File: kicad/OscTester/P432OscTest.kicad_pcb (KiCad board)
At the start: 2 copper layers, 49.5 x 59.7 mm, 12 parts, among them J1 Power-XP6, J2 Freq-XP1, J3 Filter-XP7, J4 Volume-XP6, J5 Control-XP5, SW1 SW_DIP_x04

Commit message: pcb fix
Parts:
- moved J1 7.62 mm to (43.2, 94.0), turned to 270 degrees
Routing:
- net +5V: track 169.9 -> 157.1 mm
- net GND: track 119.4 -> 121.8 mm
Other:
- board text added: "1"
- board text added: "11"
- board text added: "4"
- board text added: "8"
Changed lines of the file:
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@@
   (general
     (thickness 1.6)
-    (drawings 33)
-    (tracks 51)
+    (drawings 43)
+    (tracks 50)
     (zones 0)
     (modules 12)
@@
   )
   (module Connector_PinSocket_2.54mm:PinSocket_1x04_P2.54mm_Vertical (layer F.Cu)
-    (at 35.56 93.98 90)
+    (at 43.18 93.98 270)
     (descr "Through hole straight socket strip, 1x04, 2.54mm pitch, single row (from Kicad 4.0.7), script generated")
     (tags "Through hole socket strip THT 1x04 2.54mm single row")
@@
       (effects (font (size 1 1) (thickness 0.15)))
     )
-    (fp_text value Power-XP6 (at -3.175 3.81 180) (layer F.SilkS)
+    (fp_text value Power-XP6 (at 2.54 3.81 180) (layer F.SilkS)
       (effects (font (size 1 1) (thickness 0.15)))
     )
@@
     (fp_line (start 0.635 -1.27) (end 1.27 -0.635) (layer F.Fab) (width 0.1))
     (fp_line (start -1.27 -1.27) (end 0.635 -1.27) (layer F.Fab) (width 0.1))
-    (pad 4 thru_hole oval (at 0 7.62 90) (size 1.7 1.7) (drill 1) (layers *.Cu *.Mask)
-      (net 1 GND))
-    (pad 3 thru_hole oval (at 0 5.08 90) (size 1.7 1.7) (drill 1) (layers *.Cu *.Mask)
-      (net 1 GND))
-    (pad 2 thru_hole oval (at 0 2.54 90) (size 1.7 1.7) (drill 1) (layers *.Cu *.Mask)
+    (pad 4 thru_hole oval (at 0 7.62 270) (size 1.7 1.7) (drill 1) (layers *.Cu *.Mask)
+      (net 1 GND))
+    (pad 3 thru_hole oval (at 0 5.08 270) (size 1.7 1.7) (drill 1) (layers *.Cu *.Mask)
+      (net 1 GND))
+    (pad 2 thru_hole oval (at 0 2.54 270) (size 1.7 1.7) (drill 1) (layers *.Cu *.Mask)
       (net 2 +5V))
-    (pad 1 thru_hole rect (at 0 0 90) (size 1.7 1.7) (drill 1) (layers *.Cu *.Mask)
+    (pad 1 thru_hole rect (at 0 0 270) (size 1.7 1.7) (drill 1) (layers *.Cu *.Mask)
       (net 2 +5V))
     (model ${KISYS3DMOD}/Connector_PinSocket_2.54mm.3dshapes/PinSocket_1x04_P2.54mm_Vertical.wrl
@@
     )
   )
-  (gr_text GND (at 41.91 91.44) (layer F.SilkS)
-    (effects (font (size 1 1) (thickness 0.15)))
-  )
-  (gr_text +5V (at 36.195 91.44) (layer F.SilkS)
+  (gr_text 4 (at 34.925 91.44) (layer F.SilkS)
+    (effects (font (size 1 1) (thickness 0.25)))
+  )
+  (gr_text 1 (at 43.815 91.44) (layer F.SilkS)
+    (effects (font (size 1 1) (thickness 0.25)))
+  )
+  (gr_text 11 (at 48.26 76.2) (layer F.SilkS)
+    (effects (font (size 1 1) (thickness 0.25)))
+  )
+  (gr_text 1 (at 73.66 76.2) (layer F.SilkS)
+    (effects (font (size 1 1) (thickness 0.25)))
+  )
+  (gr_text 8 (at 55.245 66.04) (layer F.SilkS)
+    (effects (font (size 1 1) (thickness 0.25)))
+  )
+  (gr_text 1 (at 73.66 66.04) (layer F.SilkS)
+    (effects (font (size 1 1) (thickness 0.25)))
+  )
+  (gr_text 8 (at 55.245 55.88) (layer F.SilkS)
+    (effects (font (size 1 1) (thickness 0.25)))
+  )
+  (gr_text 1 (at 73.66 55.88) (layer F.SilkS)
+    (effects (font (size 1 1) (thickness 0.25)))
+  )
+  (gr_text 8 (at 55.88 45.72) (layer F.SilkS)
+    (effects (font (size 1 1) (thickness 0.25)))
+  )
+  (gr_text 1 (at 74.295 45.72) (layer F.SilkS)
+    (effects (font (size 1 1) (thickness 0.25)))
+  )
+  (gr_text GND (at 37.465 91.44) (layer F.SilkS)
+    (effects (font (size 1 1) (thickness 0.15)))
+  )
+  (gr_text +5V (at 41.275 91.44) (layer F.SilkS)
     (effects (font (size 1 1) (thickness 0.15)))
   )
@@
   (segment (start 63.5 78.74) (end 48.26 78.74) (width 0.8) (layer B.Cu) (net 1))
   (segment (start 48.26 78.74) (end 45.72 78.74) (width 0.8) (layer B.Cu) (net 1))
-  (segment (start 43.18 81.28) (end 43.18 93.98) (width 0.8) (layer B.Cu) (net 1))
-  (segment (start 45.72 78.74) (end 43.18 81.28) (width 0.8) (layer B.Cu) (net 1))
-  (segment (start 43.18 93.98) (end 40.64 93.98) (width 0.8) (layer B.Cu) (net 1))
   (segment (start 71.12 48.26) (end 55.88 48.26) (width 0.8) (layer B.Cu) (net 1))
   (segment (start 38.1 49.53) (end 38.1 58.42) (width 0.8) (layer B.Cu) (net 1))
@@
   (segment (start 38.1 58.42) (end 38.1 68.58) (width 0.8) (layer B.Cu) (net 1))
   (segment (start 38.1 68.58) (end 38.1 76.2) (width 0.8) (layer B.Cu) (net 1))
-  (segment (start 38.1 76.2) (end 43.18 81.28) (width 0.8) (layer B.Cu) (net 1))
-  (segment (start 35.56 93.98) (end 38.1 93.98) (width 0.8) (layer B.Cu) (net 2))
+  (segment (start 35.56 93.98) (end 38.1 93.98) (width 0.8) (layer B.Cu) (net 1))
+  (segment (start 38.1 93.98) (end 38.1 86.36) (width 0.8) (layer B.Cu) (net 1))
+  (segment (start 45.72 78.74) (end 39.37 78.74) (width 0.8) (layer B.Cu) (net 1))
+  (segment (start 38.1 76.2) (end 38.1 80.01) (width 0.8) (layer B.Cu) (net 1))
+  (segment (start 39.37 78.74) (end 38.1 80.01) (width 0.8) (layer B.Cu) (net 1))
+  (segment (start 38.1 80.01) (end 38.1 86.36) (width 0.8) (layer B.Cu) (net 1))
   (segment (start 73.66 93.98) (end 66.04 93.98) (width 0.8) (layer B.Cu) (net 2))
-  (segment (start 66.04 93.98) (end 63.5 93.98) (width 0.8) (layer B.Cu) (net 2))
-  (segment (start 63.5 93.98) (end 58.42 99.06) (width 0.8) (layer B.Cu) (net 2))
-  (segment (start 35.56 95.63) (end 35.56 93.98) (width 0.8) (layer B.Cu) (net 2))
-  (segment (start 38.99 99.06) (end 35.56 95.63) (width 0.8) (layer B.Cu) (net 2))
-  (segment (start 58.42 99.06) (end 38.99 99.06) (width 0.8) (layer B.Cu) (net 2))
   (segment (start 73.66 93.98) (end 76.2 93.98) (width 0.8) (layer B.Cu) (net 2))
   (segment (start 76.2 93.98) (end 77.47 92.71) (width 0.8) (layer B.Cu) (net 2))
@@
   (segment (start 48.26 63.5) (end 43.18 68.58) (width 0.8) (layer B.Cu) (net 2))
   (segment (start 77.47 92.71) (end 77.47 63.5) (width 0.8) (layer B.Cu) (net 2))
+  (segment (start 63.5 93.98) (end 43.18 93.98) (width 0.8) (layer B.Cu) (net 2))
+  (segment (start 66.04 93.98) (end 63.5 93.98) (width 0.8) (layer B.Cu) (net 2))
+  (segment (start 43.18 93.98) (end 40.64 93.98) (width 0.8) (layer B.Cu) (net 2))
   (segment (start 66.04 76.2) (end 66.04 78.74) (width 0.8) (layer B.Cu) (net 3))
   (segment (start 66.04 78.74) (end 66.04 86.36) (width 0.8) (layer B.Cu) (net 3))

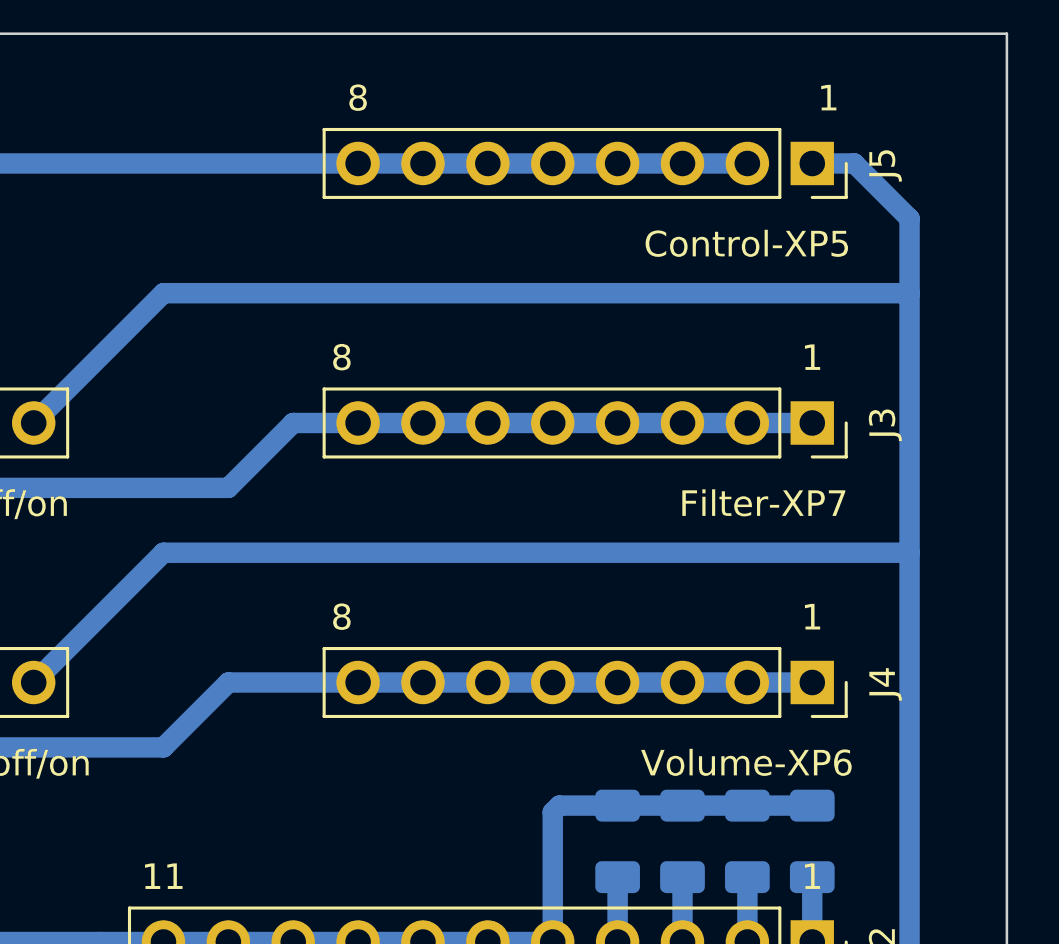
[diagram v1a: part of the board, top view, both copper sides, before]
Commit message: Unison bit set to 0 to test all 8 voices
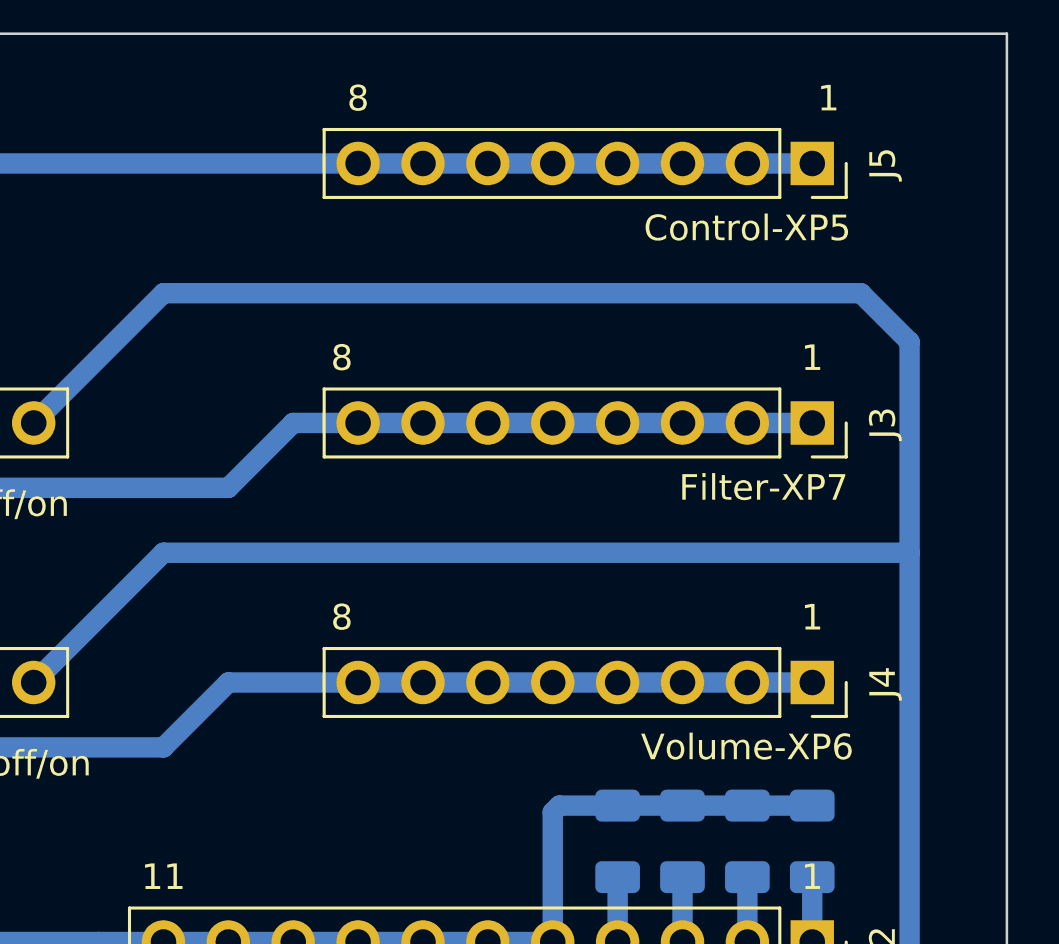
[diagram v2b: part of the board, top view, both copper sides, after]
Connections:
- net /FC0 renamed /1
- net /FC1 renamed /2
- net /FC2 renamed /3
- net /FC3 renamed /4
- J5 pad 1: +5V -> GND
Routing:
- net +5V: track 157.1 -> 148.4 mm
- net GND: track 121.8 -> 124.3 mm

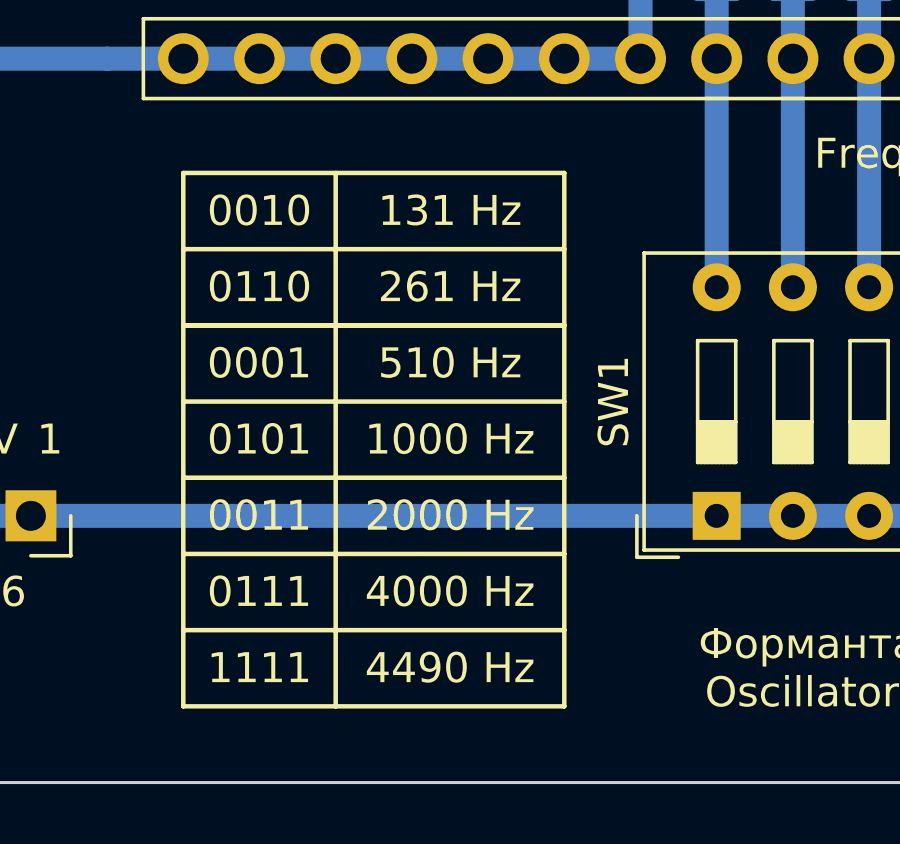
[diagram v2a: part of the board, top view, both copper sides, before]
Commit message: Freq values changed to the correct ones.
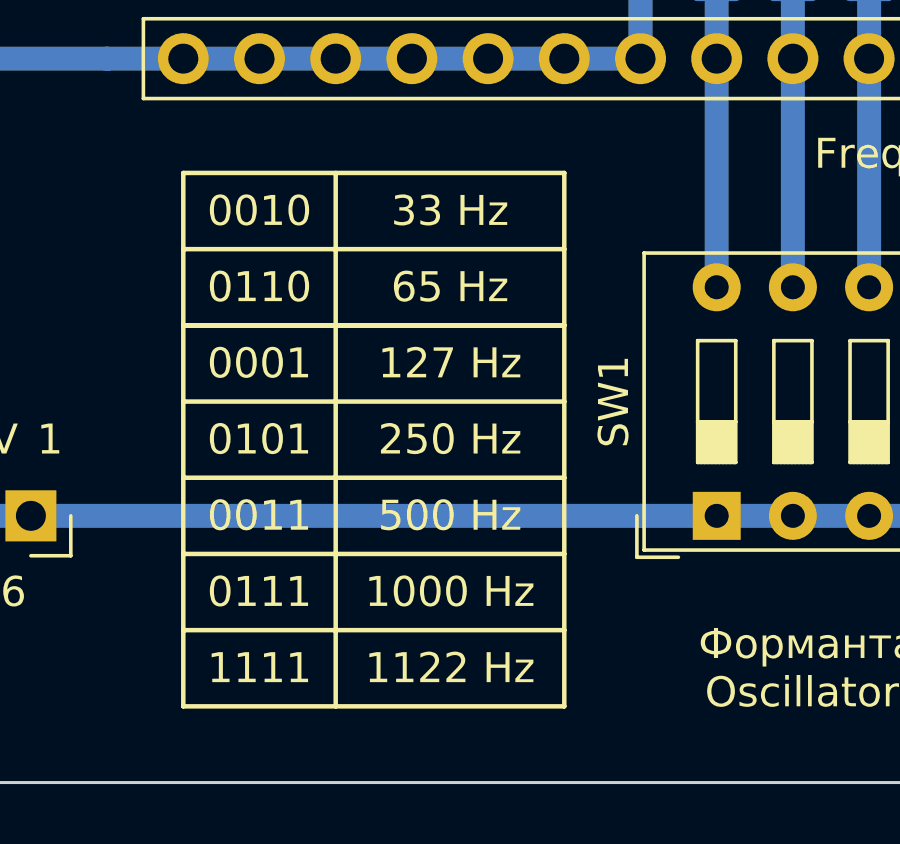
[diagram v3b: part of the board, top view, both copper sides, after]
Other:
- board text added: "1122 Hz"
- board text added: "127 Hz"
- board text added: "250 Hz"
- board text added: "33 Hz"
- board text added: "500 Hz"
- board text added: "65 Hz"
- board text removed: "131 Hz"
- board text removed: "2000 Hz"
- board text removed: "261 Hz"
- board text removed: "4000 Hz"
- board text removed: "4490 Hz"
- board text removed: "510 Hz"
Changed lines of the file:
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@@
     (effects (font (size 1 1) (thickness 0.15)))
   )
-  (gr_text "131 Hz" (at 57.15 83.82) (layer F.SilkS)
+  (gr_text "33 Hz" (at 57.15 83.82) (layer F.SilkS)
     (effects (font (size 1 1) (thickness 0.15)))
   )
-  (gr_text "261 Hz" (at 57.15 86.36) (layer F.SilkS)
+  (gr_text "65 Hz" (at 57.15 86.36) (layer F.SilkS)
     (effects (font (size 1 1) (thickness 0.15)))
   )
@@
   (gr_line (start 48.26 87.63) (end 60.96 87.63) (layer F.SilkS) (width 0.15))
   (gr_line (start 48.26 85.09) (end 60.96 85.09) (layer F.SilkS) (width 0.15))
-  (gr_text "4490 Hz" (at 57.15 99.06) (layer F.SilkS)
+  (gr_text "1122 Hz" (at 57.15 99.06) (layer F.SilkS)
     (effects (font (size 1 1) (thickness 0.15)))
   )
@@
   )
   (gr_line (start 48.26 97.79) (end 60.96 97.79) (layer F.SilkS) (width 0.15))
-  (gr_text "4000 Hz" (at 57.15 96.52) (layer F.SilkS)
+  (gr_text "1000 Hz" (at 57.15 96.52) (layer F.SilkS)
     (effects (font (size 1 1) (thickness 0.15)))
   )
@@
   )
   (gr_line (start 48.26 95.25) (end 60.96 95.25) (layer F.SilkS) (width 0.15))
-  (gr_text "2000 Hz" (at 57.15 93.98) (layer F.SilkS)
+  (gr_text "500 Hz" (at 57.15 93.98) (layer F.SilkS)
     (effects (font (size 1 1) (thickness 0.15)))
   )
@@
   )
   (gr_line (start 48.26 92.71) (end 60.96 92.71) (layer F.SilkS) (width 0.15))
-  (gr_text "1000 Hz" (at 57.15 91.44) (layer F.SilkS)
+  (gr_text "250 Hz" (at 57.15 91.44) (layer F.SilkS)
     (effects (font (size 1 1) (thickness 0.15)))
   )
@@
   )
   (gr_line (start 48.26 90.17) (end 60.96 90.17) (layer F.SilkS) (width 0.15))
-  (gr_text "510 Hz" (at 57.15 88.9) (layer F.SilkS)
+  (gr_text "127 Hz" (at 57.15 88.9) (layer F.SilkS)
     (effects (font (size 1 1) (thickness 0.15)))
   )
@@
   (segment (start 75.565 53.34) (end 48.26 53.34) (width 0.8) (layer B.Cu) (net 2))
   (segment (start 77.47 55.245) (end 75.565 53.34) (width 0.8) (layer B.Cu) (net 2))
-  (segment (start 66.04 76.2) (end 66.04 78.74) (width 0.8) (layer B.Cu) (net 5))
-  (segment (start 66.04 78.74) (end 66.04 86.36) (width 0.8) (layer B.Cu) (net 5))
-  (segment (start 68.58 76.2) (end 68.58 78.74) (width 0.8) (layer B.Cu) (net 6))
-  (segment (start 68.58 78.74) (end 68.58 86.36) (width 0.8) (layer B.Cu) (net 6))
-  (segment (start 71.12 76.2) (end 71.12 78.74) (width 0.8) (layer B.Cu) (net 7))
-  (segment (start 71.12 78.74) (end 71.12 86.36) (width 0.8) (layer B.Cu) (net 7))
-  (segment (start 73.66 76.2) (end 73.66 78.74) (width 0.8) (layer B.Cu) (net 8))
-  (segment (start 73.66 78.74) (end 73.66 86.36) (width 0.8) (layer B.Cu) (net 8))
   (segment (start 73.66 58.42) (end 55.88 58.42) (width 0.8) (layer B.Cu) (net 3))
   (segment (start 55.88 58.42) (end 53.34 58.42) (width 0.8) (layer B.Cu) (net 3))
@@
   (segment (start 40.64 71.12) (end 40.64 68.58) (width 0.8) (layer B.Cu) (net 4))
   (segment (start 50.8 68.58) (end 48.26 71.12) (width 0.8) (layer B.Cu) (net 4))
+  (segment (start 66.04 76.2) (end 66.04 78.74) (width 0.8) (layer B.Cu) (net 5))
+  (segment (start 66.04 78.74) (end 66.04 86.36) (width 0.8) (layer B.Cu) (net 5))
+  (segment (start 68.58 76.2) (end 68.58 78.74) (width 0.8) (layer B.Cu) (net 6))
+  (segment (start 68.58 78.74) (end 68.58 86.36) (width 0.8) (layer B.Cu) (net 6))
+  (segment (start 71.12 76.2) (end 71.12 78.74) (width 0.8) (layer B.Cu) (net 7))
+  (segment (start 71.12 78.74) (end 71.12 86.36) (width 0.8) (layer B.Cu) (net 7))
+  (segment (start 73.66 76.2) (end 73.66 78.74) (width 0.8) (layer B.Cu) (net 8))
+  (segment (start 73.66 78.74) (end 73.66 86.36) (width 0.8) (layer B.Cu) (net 8))
 )
